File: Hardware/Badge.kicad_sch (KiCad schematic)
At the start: 67 parts, among them J1 Battery_Conn, J2 Conn_01x02, J3 DEBUG, J4 Conn_02x15_Counter_Clockwise, P1 USB_C_Plug_USB2.0, Q1 SI1967DH-T1-GE3, Q2 2SC4213, SW1 BOOT_MODE, SW2 RESET, SW3 PWR_BATT, SW4 SEL_BATT, SW5 Button B, SW6 Button A, U1 W25Q128JVS, U2 MCP73832-2-OT, U3 LD1117S33TR_SOT223, U4 RP2040, X1 Simple_Addon_v2, Y1 12MHz_GND24

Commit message: Inverted TX/RX from ESP32 - added INT line from BHI - Changed ESP32 dbg port to bigger footprint
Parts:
- added R21 (x2), R22: 4.7k, Resistor_SMD:R_0402_1005Metric, symbol Device:R
- J2: footprint Connector_PinSocket_1.00mm:PinSocket_1x04_P1.00mm_Vertical -> Connector_PinSocket_1.27mm:PinSocket_1x04_P1.27mm_Vertical
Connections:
- net +3V3: now also R21.1, R21.1, R22.1
- net ESP_RX: now also U4.27 (GPIO16); no longer U4.28 (GPIO17)
- net ESP_TX: now also U4.28 (GPIO17); no longer U4.27 (GPIO16)
- net I2C_SCL: now also R21.2
- net I2C_SDA: now also R22.2
- net GPIO_15: no longer names the net of J4.21 (Pin_21)
- net GPIO_15: no longer U4.18 (GPIO15)
- new net INT: R21.2, U4.18 (GPIO15)
- no-connect marks 7 -> 6

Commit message: First modification for v2
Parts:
- removed BT1: Battery_Cell, Battery:BatteryHolder_LINX_BAT-HLD-012-SMT, symbol Device:Battery_Cell
- removed D16: D_Schottky, Diode_SMD:D_SMA, symbol Device:D_Schottky
- removed J2: Conn_01x02, Connector_PinSocket_1.27mm:PinSocket_1x04_P1.27mm_Vertical, symbol Connector_Generic:Conn_01x04
- removed R12, R8, R9: 10k, Resistor_SMD:R_0402_1005Metric, symbol Device:R
- removed R21 (x2), R22: 4.7k, Resistor_SMD:R_0402_1005Metric, symbol Device:R
- removed SW4: SEL_BATT, Button_Switch_SMD:SW_SPDT_CK-JS102011SAQN, symbol Switch:SW_SPDT
- added J6: Internal_I2C, Connector_PinHeader_1.00mm:PinHeader_1x03_P1.00mm_Vertical, symbol Connector:Conn_01x03_Pin
- added R21: 10k, Resistor_SMD:R_0402_1005Metric, symbol Device:R
- added R21 (x2), R22 (x2): 4.7k, Resistor_SMD:R_0402_1005Metric, symbol Device:R
- J3: footprint Connector_PinSocket_2.54mm:PinSocket_1x03_P2.54mm_Vertical -> Connector_PinHeader_1.27mm:PinHeader_1x03_P1.27mm_Vertical
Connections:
- net +3V3: now also R21.1, R21.1, R21.2, R22.1, R22.1
- net ESP_EN: no longer R14.1
- net ESP_RX: now also R14.1
- net ESP_TX: now also R21.1
- net GPIO_14: no longer U4.17 (GPIO14)
- net I2C_SCL: now also R22.2
- net I2C_SDA: now also R22.2
- net at SW3.1 (A), U2.3 (VBAT): now also J1.2 (Pin_2)
- net INT renamed SEN_INT
- net SEN_INT: now also R21.2
- new net Gyros/INT_INT: J6.3 (Pin_3)
- new net Gyros/INT_SCK: J6.2 (Pin_2)
- new net Gyros/INT_SDA: J6.1 (Pin_1)
- new net NFC_INT: R21.2, U4.17 (GPIO14)
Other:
- added sheet NFC (NFC.kicad_sch)
- sheet Gyros ports: added INT_INT, INT_SCK, INT_SDA; removed none
- note added: "ESP32"
- note added: "Front Buttons"
- note added: "NFC"
- note added: "PullUp Resistors"
- note added: "WARNING: CHECK THE ESP32 BOOT PIN NEEDS FOR FUNCTIONING"
- note removed: "Buttons"
- note removed: "ESP32 Prog"
- note removed: "WiFi & BT"
- moved on the sheet: J1, SW5, SW6

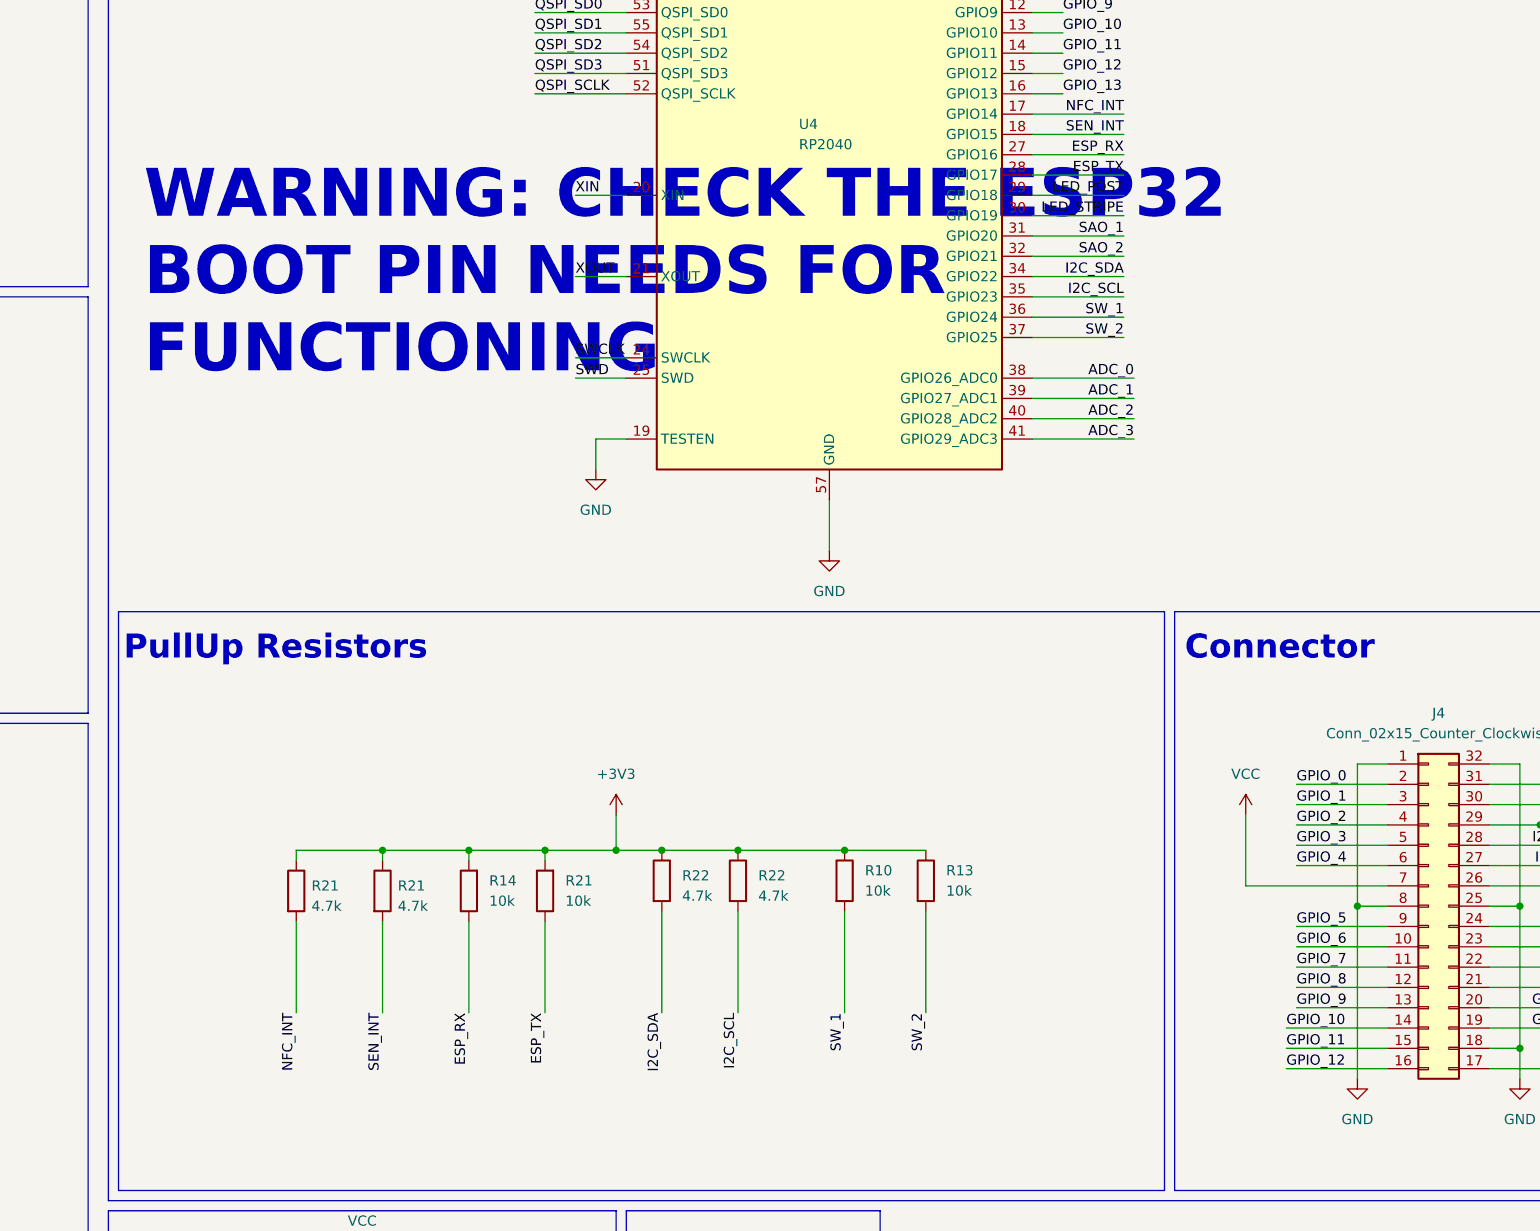
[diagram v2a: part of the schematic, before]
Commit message: WIP - Added NFC Antenna and connected almost everythings else
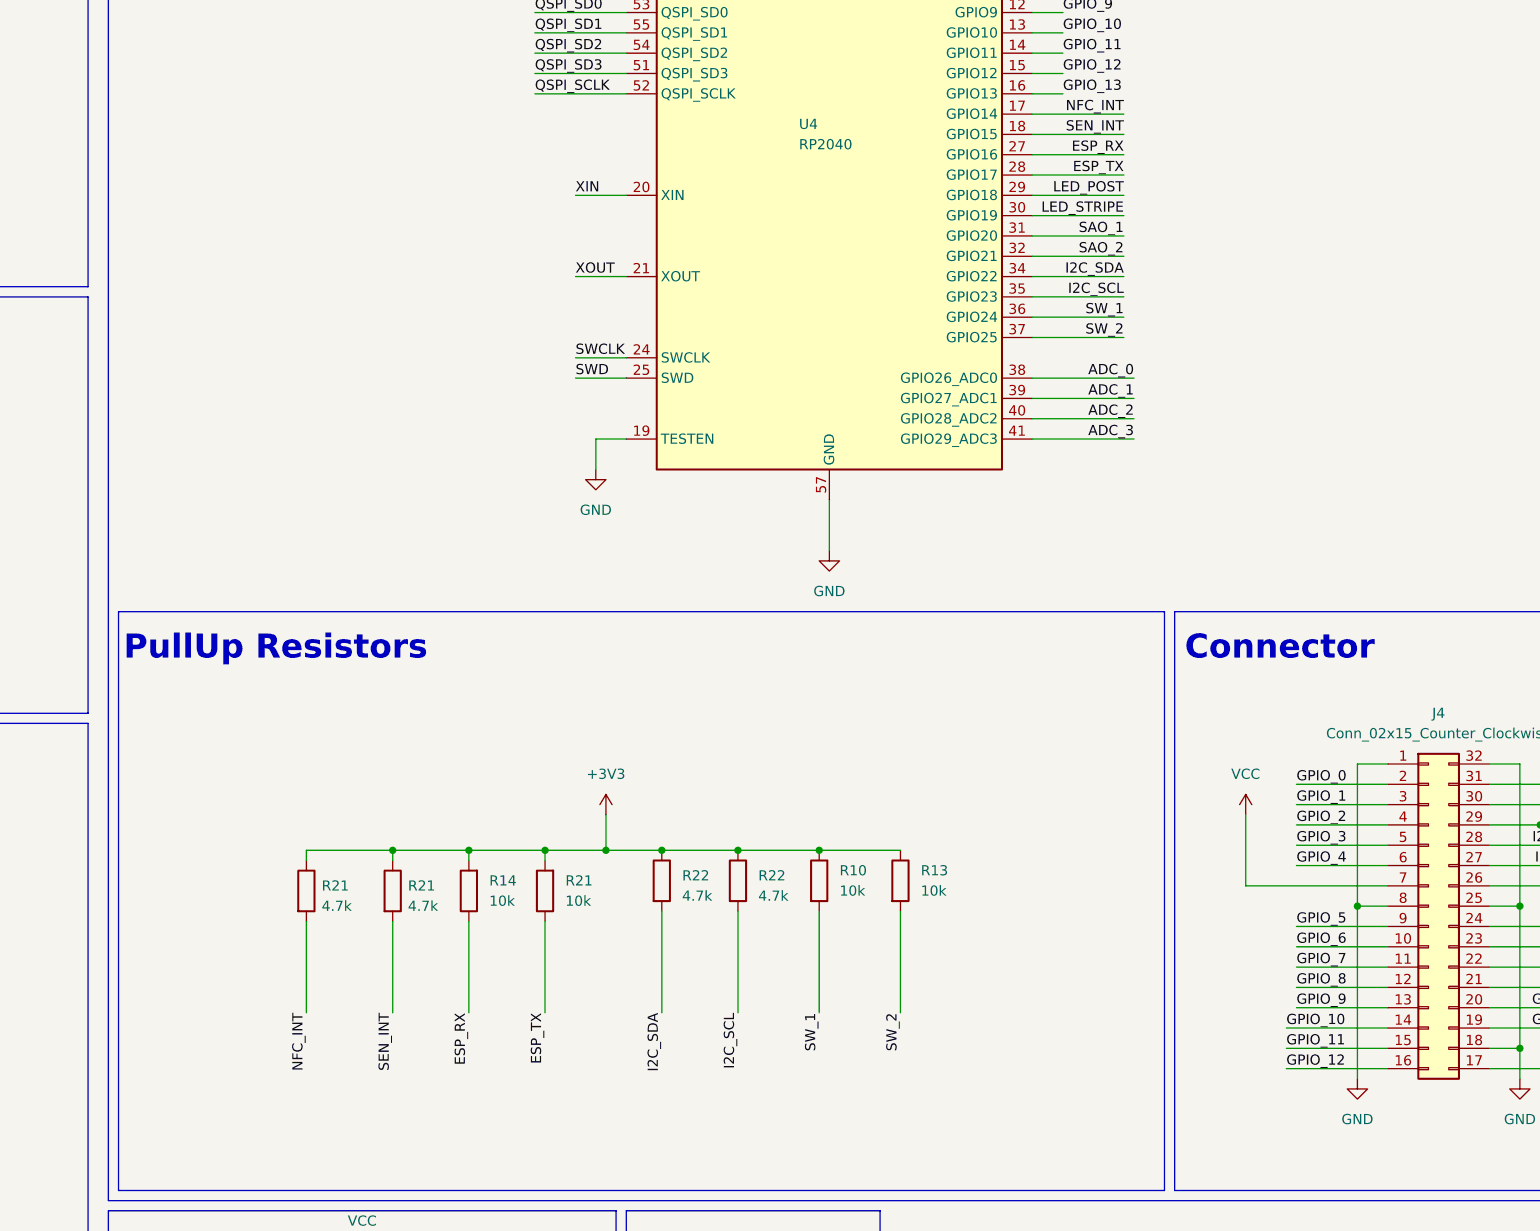
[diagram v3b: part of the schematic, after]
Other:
- note removed: "WARNING: CHECK THE ESP32 BOOT PIN NEEDS FOR FUNCTIONING"
- moved on the sheet: R10, R13, R21
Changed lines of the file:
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@@
   (junction (at 378.46 232.41) (diameter 0) (color 0 0 0 0)
   )
-  (junction (at 294.005 207.645) (diameter 0) (color 0 0 0 0)
+  (junction (at 290.83 207.645) (diameter 0) (color 0 0 0 0)
   )
   (junction (at 82.55 176.53) (diameter 0) (color 0 0 0 0)
@@
   (junction (at 52.07 152.4) (diameter 0) (color 0 0 0 0)
   )
+  (junction (at 264.16 207.645) (diameter 0) (color 0 0 0 0)
+  )
   (junction (at 294.64 66.04) (diameter 0) (color 0 0 0 0)
   )
@@
   (junction (at 392.43 76.2) (diameter 0) (color 0 0 0 0)
   )
-  (junction (at 265.43 207.645) (diameter 0) (color 0 0 0 0)
-  )
   (junction (at 189.23 67.31) (diameter 0) (color 0 0 0 0)
   )
@@
   (junction (at 392.43 63.5) (diameter 0) (color 0 0 0 0)
   )
-  (junction (at 236.22 207.645) (diameter 0) (color 0 0 0 0)
+  (junction (at 237.49 207.645) (diameter 0) (color 0 0 0 0)
   )
   (junction (at 262.89 49.53) (diameter 0) (color 0 0 0 0)
@@
     (stroke (width 0) (type default))
   )
-  (wire (pts (xy 294.005 227.965) (xy 294.005 215.265))
+  (wire (pts (xy 290.83 227.965) (xy 290.83 215.265))
     (stroke (width 0) (type default))
   )
@@
     (stroke (width 0) (type solid))
   )
-  (wire (pts (xy 225.425 207.645) (xy 225.425 208.915))
+  (wire (pts (xy 226.695 207.645) (xy 226.695 208.915))
     (stroke (width 0) (type default))
   )
@@
     (stroke (width 0) (type default))
   )
-  (wire (pts (xy 236.22 216.535) (xy 236.22 227.965))
+  (wire (pts (xy 237.49 216.535) (xy 237.49 227.965))
     (stroke (width 0) (type default))
   )
@@
     (stroke (width 0) (type solid))
   )
-  (wire (pts (xy 265.43 203.2) (xy 265.43 207.645))
+  (wire (pts (xy 264.16 203.2) (xy 264.16 207.645))
     (stroke (width 0) (type default))
   )
@@
     (stroke (width 0) (type default))
   )
-  (wire (pts (xy 265.43 207.645) (xy 271.145 207.645))
-    (stroke (width 0) (type default))
-  )
   (wire (pts (xy 64.77 44.45) (xy 64.77 43.18))
     (stroke (width 0) (type default))
@@
     (stroke (width 0) (type default))
   )
-  (wire (pts (xy 236.22 207.645) (xy 247.015 207.645))
+  (wire (pts (xy 237.49 207.645) (xy 247.015 207.645))
     (stroke (width 0) (type default))
   )
@@
     (stroke (width 0) (type default))
   )
-  (wire (pts (xy 280.67 207.645) (xy 294.005 207.645))
+  (wire (pts (xy 280.67 207.645) (xy 290.83 207.645))
     (stroke (width 0) (type default))
   )
@@
     (stroke (width 0) (type default))
   )
-  (wire (pts (xy 256.54 207.645) (xy 265.43 207.645))
+  (wire (pts (xy 256.54 207.645) (xy 264.16 207.645))
     (stroke (width 0) (type default))
   )
@@
     (stroke (width 0) (type default))
   )
-  (wire (pts (xy 294.005 207.645) (xy 304.165 207.645))
+  (wire (pts (xy 290.83 207.645) (xy 300.99 207.645))
     (stroke (width 0) (type default))
   )
@@
     (stroke (width 0) (type default))
   )
-  (wire (pts (xy 225.425 207.645) (xy 236.22 207.645))
+  (wire (pts (xy 226.695 207.645) (xy 237.49 207.645))
     (stroke (width 0) (type default))
   )
@@
     (stroke (width 0) (type default))
   )
-  (wire (pts (xy 304.165 227.965) (xy 304.165 215.265))
+  (wire (pts (xy 300.99 227.965) (xy 300.99 215.265))
     (stroke (width 0) (type default))
   )
@@
     (stroke (width 0) (type default))
   )
-  (wire (pts (xy 225.425 216.535) (xy 225.425 227.965))
+  (wire (pts (xy 226.695 216.535) (xy 226.695 227.965))
     (stroke (width 0) (type default))
   )
@@
     (stroke (width 0) (type default))
   )
-  (wire (pts (xy 236.22 207.645) (xy 236.22 208.915))
+  (wire (pts (xy 237.49 207.645) (xy 237.49 208.915))
     (stroke (width 0) (type default))
   )
@@
     (stroke (width 0) (type default))
   )
+  (wire (pts (xy 264.16 207.645) (xy 271.145 207.645))
+    (stroke (width 0) (type default))
+  )
   (image (at 322.58 260.35) (scale 1.02042)
     (data
@@
     (effects (font (size 3 3) (thickness 0.6) bold) (justify left bottom))
   )
-  (text "WARNING: CHECK THE ESP32\nBOOT PIN NEEDS FOR \nFUNCTIONING "
-    (at 206.375 148.59 0)
-    (effects (font (size 6 6) (thickness 1.2) bold) (justify left bottom))
-  )
   (text "This two resistors can be removed" (at 304.8 38.1 0)
     (effects (font (size 1.27 1.27)) (justify left bottom))
@@
     (effects (font (size 1.27 1.27)) (justify left bottom))
   )
-  (label "SW_2" (at 304.165 227.965 270) (fields_autoplaced)
+  (label "SW_2" (at 300.99 227.965 270) (fields_autoplaced)
     (effects (font (size 1.27 1.27)) (justify right bottom))
   )
@@
     (effects (font (size 1.27 1.27)) (justify left bottom))
   )
-  (label "SEN_INT" (at 236.22 227.965 270) (fields_autoplaced)
+  (label "SEN_INT" (at 237.49 227.965 270) (fields_autoplaced)
     (effects (font (size 1.27 1.27)) (justify right bottom))
   )
@@
     (effects (font (size 1.27 1.27)) (justify right bottom))
   )
-  (label "SW_1" (at 294.005 227.965 270) (fields_autoplaced)
+  (label "SW_1" (at 290.83 227.965 270) (fields_autoplaced)
     (effects (font (size 1.27 1.27)) (justify right bottom))
   )
@@
     (effects (font (size 1.27 1.27)) (justify right bottom))
   )
-  (label "NFC_INT" (at 225.425 227.965 270) (fields_autoplaced)
+  (label "NFC_INT" (at 226.695 227.965 270) (fields_autoplaced)
     (effects (font (size 1.27 1.27)) (justify right bottom))
   )
@@
     )
   )
-  (symbol (lib_id "Device:R") (at 236.22 212.725 0) (unit 1)
+  (symbol (lib_id "Device:R") (at 237.49 212.725 0) (unit 1)
     (in_bom yes) (on_board yes) (dnp no) (fields_autoplaced)
-    (property "Reference" "R21" (at 238.125 212.09 0)
+    (property "Reference" "R21" (at 239.395 212.09 0)
       (effects (font (size 1.27 1.27)) (justify left))
     )
-    (property "Value" "4.7k" (at 238.125 214.63 0)
+    (property "Value" "4.7k" (at 239.395 214.63 0)
       (effects (font (size 1.27 1.27)) (justify left))
     )
-    (property "Footprint" "Resistor_SMD:R_0402_1005Metric" (at 234.442 212.725 90)
+    (property "Footprint" "Resistor_SMD:R_0402_1005Metric" (at 235.712 212.725 90)
       (effects (font (size 1.27 1.27)) hide)
     )
-    (property "Datasheet" "~" (at 236.22 212.725 0)
+    (property "Datasheet" "~" (at 237.49 212.725 0)
       (effects (font (size 1.27 1.27)) hide)
     )
@@
     )
   )
-  (symbol (lib_id "Device:R") (at 225.425 212.725 0) (unit 1)
+  (symbol (lib_id "Device:R") (at 226.695 212.725 0) (unit 1)
     (in_bom yes) (on_board yes) (dnp no) (fields_autoplaced)
-    (property "Reference" "R21" (at 227.33 212.09 0)
+    (property "Reference" "R21" (at 228.6 212.09 0)
       (effects (font (size 1.27 1.27)) (justify left))
     )
-    (property "Value" "4.7k" (at 227.33 214.63 0)
+    (property "Value" "4.7k" (at 228.6 214.63 0)
       (effects (font (size 1.27 1.27)) (justify left))
     )
-    (property "Footprint" "Resistor_SMD:R_0402_1005Metric" (at 223.647 212.725 90)
+    (property "Footprint" "Resistor_SMD:R_0402_1005Metric" (at 224.917 212.725 90)
       (effects (font (size 1.27 1.27)) hide)
     )
-    (property "Datasheet" "~" (at 225.425 212.725 0)
+    (property "Datasheet" "~" (at 226.695 212.725 0)
       (effects (font (size 1.27 1.27)) hide)
     )
@@
     )
   )
-  (symbol (lib_id "Device:R") (at 304.165 211.455 0) (unit 1)
+  (symbol (lib_id "Device:R") (at 300.99 211.455 0) (unit 1)
     (in_bom yes) (on_board yes) (dnp no) (fields_autoplaced)
-    (property "Reference" "R13" (at 306.705 210.1849 0)
+    (property "Reference" "R13" (at 303.53 210.1849 0)
       (effects (font (size 1.27 1.27)) (justify left))
     )
-    (property "Value" "10k" (at 306.705 212.7249 0)
+    (property "Value" "10k" (at 303.53 212.7249 0)
       (effects (font (size 1.27 1.27)) (justify left))
     )
-    (property "Footprint" "Resistor_SMD:R_0402_1005Metric" (at 302.387 211.455 90)
+    (property "Footprint" "Resistor_SMD:R_0402_1005Metric" (at 299.212 211.455 90)
       (effects (font (size 1.27 1.27)) hide)
     )
-    (property "Datasheet" "~" (at 304.165 211.455 0)
+    (property "Datasheet" "~" (at 300.99 211.455 0)
       (effects (font (size 1.27 1.27)) hide)
     )
@@
     )
   )
-  (symbol (lib_id "power:+3V3") (at 265.43 203.2 0) (unit 1)
+  (symbol (lib_id "power:+3V3") (at 264.16 203.2 0) (unit 1)
     (in_bom yes) (on_board yes) (dnp no) (fields_autoplaced)
-    (property "Reference" "#PWR016" (at 265.43 207.01 0)
+    (property "Reference" "#PWR016" (at 264.16 207.01 0)
       (effects (font (size 1.27 1.27)) hide)
     )
-    (property "Value" "+3V3" (at 265.43 198.12 0)
+    (property "Value" "+3V3" (at 264.16 198.12 0)
       (effects (font (size 1.27 1.27)))
     )
-    (property "Footprint" "" (at 265.43 203.2 0)
+    (property "Footprint" "" (at 264.16 203.2 0)
       (effects (font (size 1.27 1.27)) hide)
     )
-    (property "Datasheet" "" (at 265.43 203.2 0)
+    (property "Datasheet" "" (at 264.16 203.2 0)
       (effects (font (size 1.27 1.27)) hide)
     )
@@
     )
   )
-  (symbol (lib_id "Device:R") (at 294.005 211.455 0) (unit 1)
+  (symbol (lib_id "Device:R") (at 290.83 211.455 0) (unit 1)
     (in_bom yes) (on_board yes) (dnp no) (fields_autoplaced)
-    (property "Reference" "R10" (at 296.545 210.1849 0)
+    (property "Reference" "R10" (at 293.37 210.1849 0)
       (effects (font (size 1.27 1.27)) (justify left))
     )
-    (property "Value" "10k" (at 296.545 212.7249 0)
+    (property "Value" "10k" (at 293.37 212.7249 0)
       (effects (font (size 1.27 1.27)) (justify left))
     )
-    (property "Footprint" "Resistor_SMD:R_0402_1005Metric" (at 292.227 211.455 90)
+    (property "Footprint" "Resistor_SMD:R_0402_1005Metric" (at 289.052 211.455 90)
       (effects (font (size 1.27 1.27)) hide)
     )
-    (property "Datasheet" "~" (at 294.005 211.455 0)
+    (property "Datasheet" "~" (at 290.83 211.455 0)
       (effects (font (size 1.27 1.27)) hide)
     )
